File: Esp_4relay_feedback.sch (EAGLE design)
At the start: 58 parts, among them IC1 LM1117MP-3.3, IC2 7805TV, IC3 7805TV, IC4 7805TV, K1 G5LE, K2 G5LE, K3 G5LE, K4 G5LE, Q1 16MHz, SW1 Push Switch, T1 BC547, T2 BC547, T3 BC547, T4 BC547, U2 ATMEGA328P_PDIP

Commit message: added 8 relays
8 relays arranged in 4 up-down manner with
esp and atmega328 at left side.

routing 70% completed.
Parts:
- removed C7, C8: 10uf, rcl:CPOL-USE2.5-6
- removed IC2: 7805TV, linear:7805TV
- removed JP5: (no value), pinhead:PINHD-1X6
- added D5, D6, D7, D8: 1N4007, diode:1N4004
- added K5, K6, K7, K8: G5LE, relay:G5LE
- added OK5, OK6, OK7, OK8: PC817, optocoupler:PC817
- added R10, R16, R18, R20: 220k, rcl:R-US_0207/10
- added R13, R17, R19, R7: 1k, rcl:R-US_0207/10
- added T5, T6, T7, T8: BC547, transistor:BC547
- added X10, X8, X9: (no value), con-wago-500:W237-103
- X5: device con-wago-500:W237-102 -> con-wago-500:W237-103; MPN (none) -> 237-103; OC_FARNELL (none) -> unknown; OC_NEWARK (none) -> 18M7116
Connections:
- removed net ESP_SUPPLY: C2.+, C8.+, IC1.IN, IC2.VO
- new net F5: OK5.COL, U2.PC3(ADC3)
- new net F6: OK6.COL, U2.PD4(XCK/T0)
- new net F7: OK7.COL, U2.PC5(ADC5/SCL)
- new net F8: OK8.COL, U2.PD2(INT0)
- new net N$34: OK5.C, R10.2
- new net N$35: R7.1, T5.B
- new net N$46: D5.A, K51.2, T5.C
- new net N$47: K62.P, OK6.A, X8-2.KL
- new net N$48: K62.S, R16.1, X8-1.KL
- new net N$49: OK6.C, R16.2
- new net N$50: R13.1, T6.B
- new net N$51: D6.A, K61.2, T6.C
- new net N$52: K72.P, OK7.A, X9-2.KL
- new net N$53: K72.S, R18.1, X9-1.KL
- new net N$54: OK7.C, R18.2
- new net N$55: R17.1, T7.B
- new net N$56: D7.A, K71.2, T7.C
- new net N$57: K82.P, OK8.A, X10-2.KL
- new net N$58: K82.S, R20.1, X10-1.KL
- new net N$59: OK8.C, R20.2
- new net N$60: R19.1, T8.B
- new net N$61: D8.A, K81.2, T8.C
- new net N$62: K52.O, X5-3.KL
- new net N$63: K62.O, X8-3.KL
- new net N$64: K72.O, X9-3.KL
- new net N$65: K82.O, X10-3.KL
- new net R5: R7.2, U2.PC2(ADC2)
- new net R6: R13.2, U2.PD5(T1)
- new net R7: R17.2, U2.PC4(ADC4/SDA)
- new net R8: R19.2, U2.PD3(INT1)
- net F1: now also U2.PB4(MISO); no longer U2.PD3(INT1)
- net F2: now also U2.PB0(ICP); no longer U2.PD5(T1)
- net F3: now also U2.PC1(ADC1); no longer U2.PD7(AIN1)
- net F4: now also U2.PD6(AIN0); no longer U2.PB1(OC1A)
- net GND: now also OK5.EMIT, OK6.EMIT, OK7.EMIT, OK8.EMIT, T5.E, T6.E, T7.E, T8.E; no longer C7.-, C8.-, IC2.GND, JP5.6, X5-2.KL
- net N$16: now also K52.P, OK5.A, X5-2.KL; no longer JP5.3, U2.PB5(SCK)
- net N$23: now also U2.PB2(SS/OC1B); no longer JP5.2, U2.PB4(MISO)
- net N$26: now also U2.PB3(MOSI/OC2); no longer C7.+, IC2.VI, X5-1.KL
- net N$32: now also K52.S, R10.1, X5-1.KL; no longer JP5.1, U2.PB3(MOSI/OC2)
- net R1: now also U2.PB5(SCK); no longer U2.PD2(INT0)
- net R2: now also U2.PB1(OC1A); no longer U2.PD4(XCK/T0)
- net R3: now also U2.PC0(ADC0); no longer U2.PD6(AIN0)
- net R4: now also U2.PD7(AIN1); no longer U2.PB0(ICP)
- net RELAY_SUPPLY: now also D5.C, D6.C, D7.C, D8.C, K51.1, K61.1, K71.1, K81.1
- net RESET: no longer JP5.4
- net VCC: now also C2.+, IC1.IN; no longer JP5.5

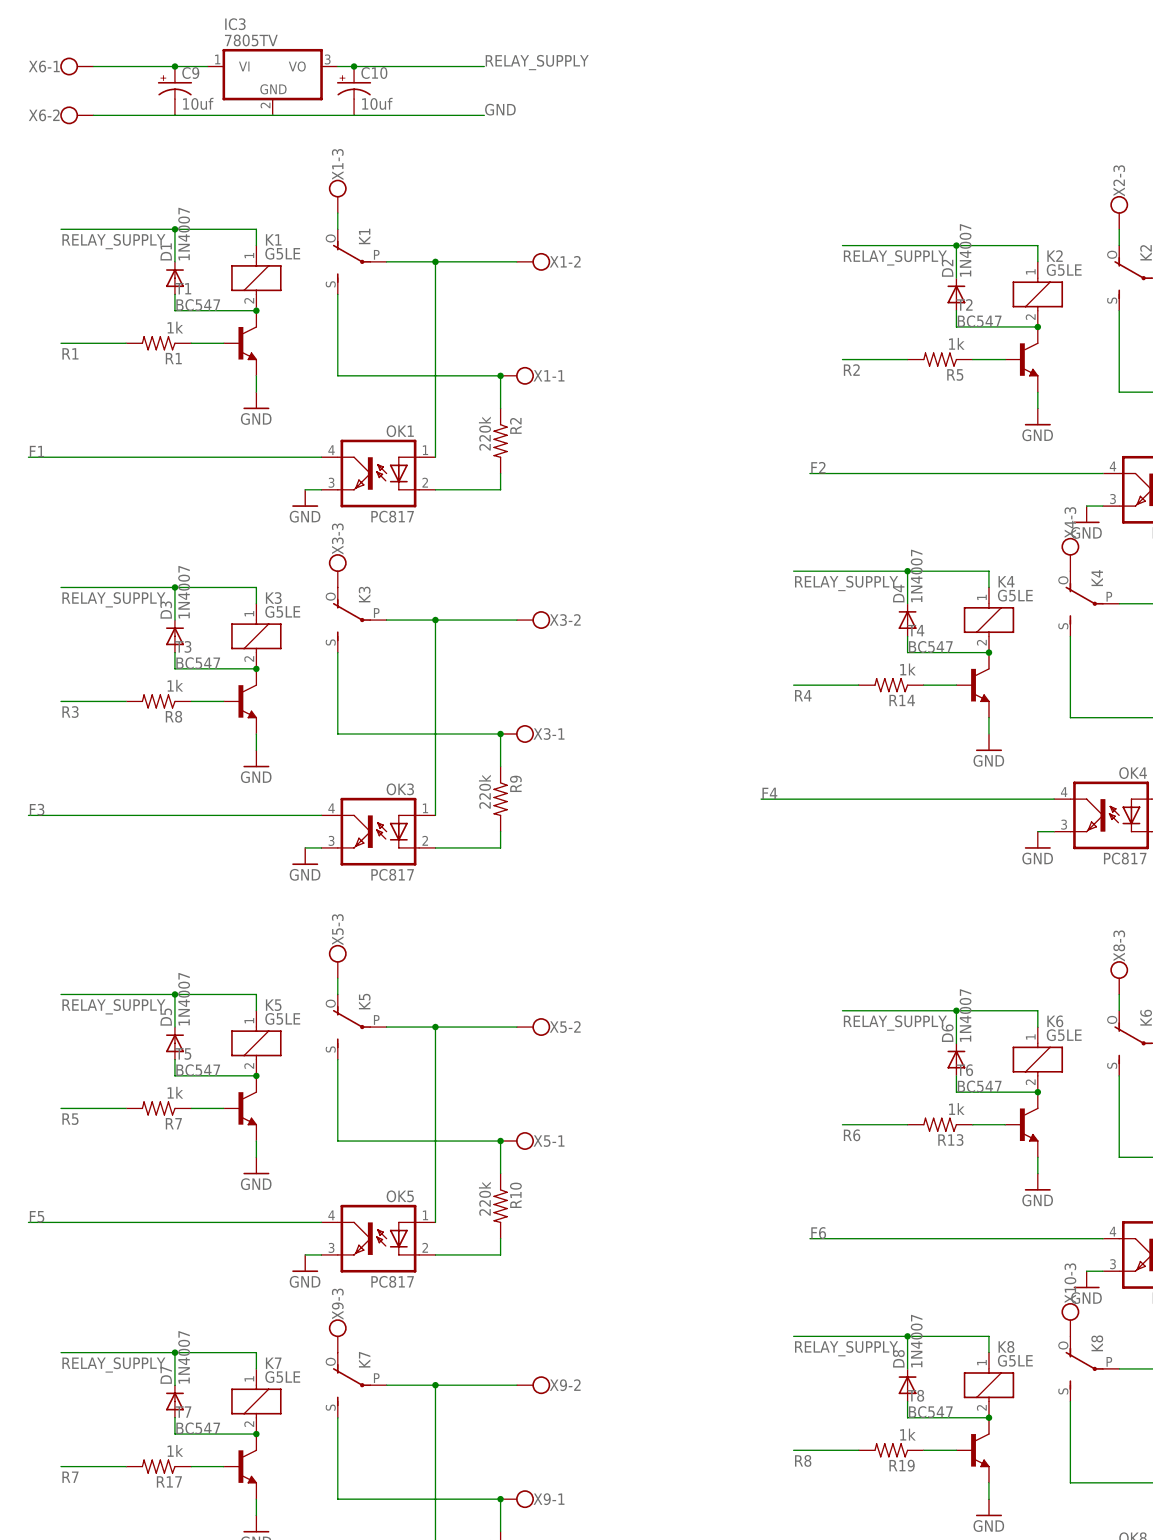
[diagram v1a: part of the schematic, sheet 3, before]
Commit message: component placing changed
Controller and esp placed in between relays.
routing done
PCB size : 130X95mm
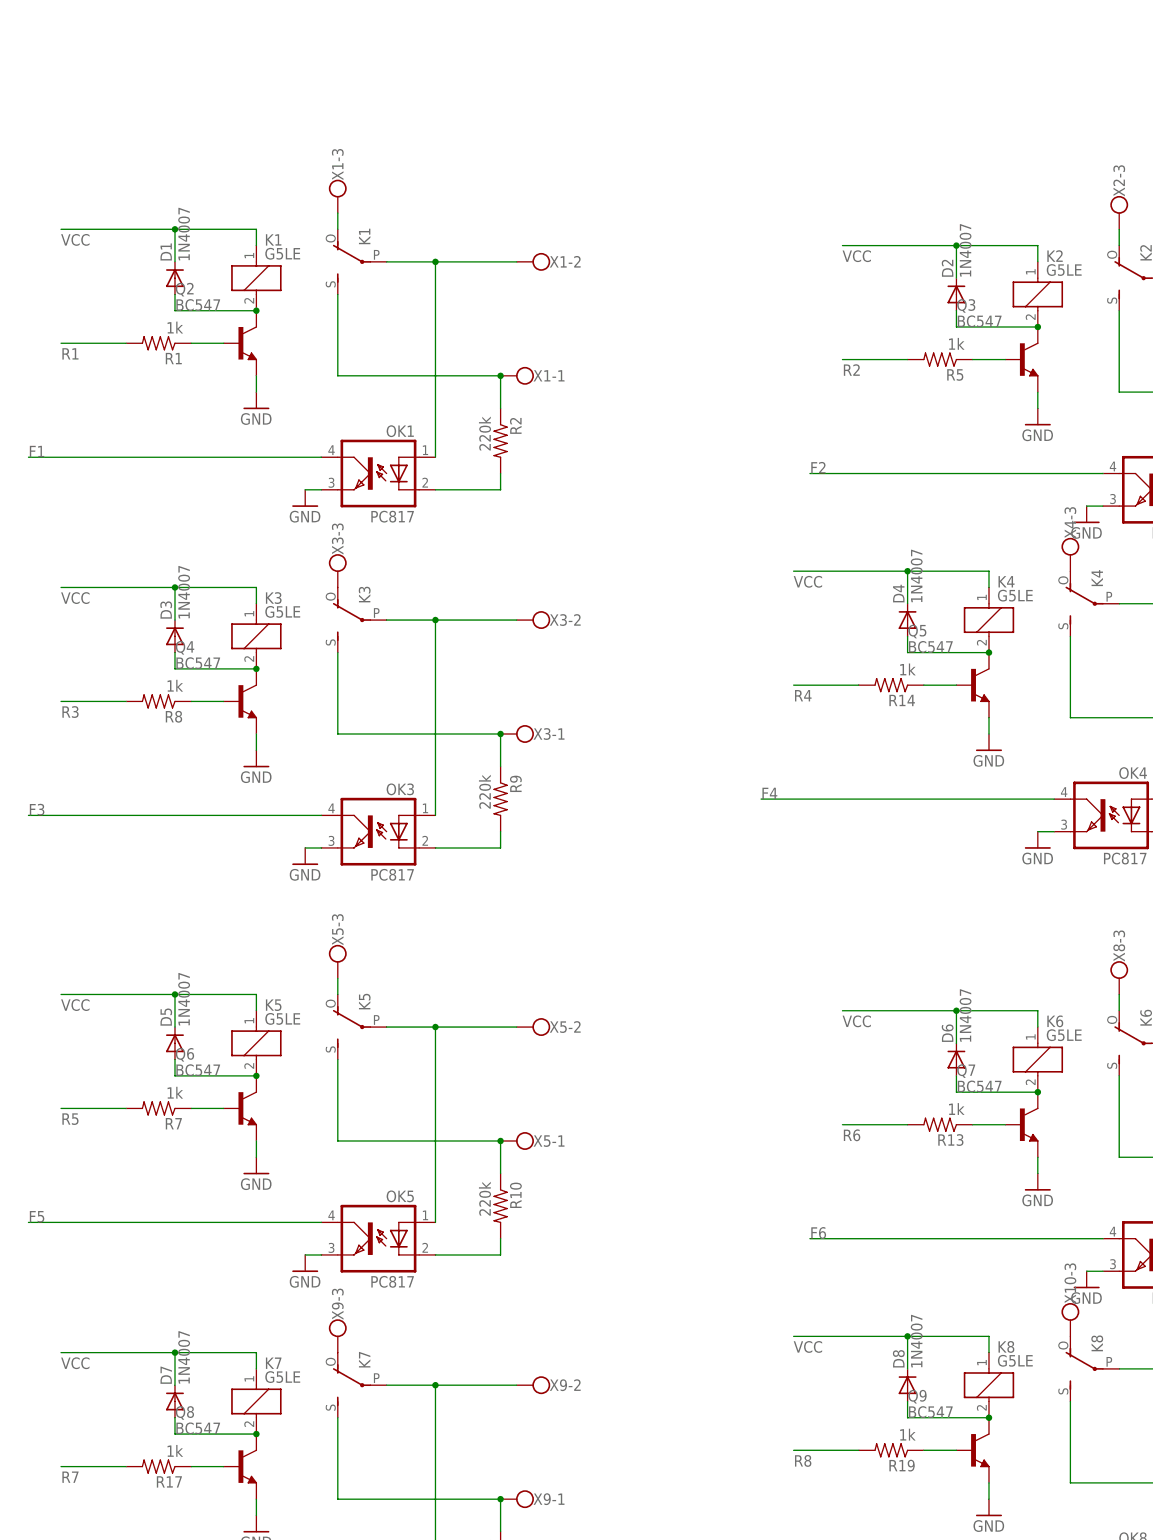
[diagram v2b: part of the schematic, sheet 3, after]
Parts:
- removed C10, C9: 10uf, rcl:CPOL-USE2.5-6
- removed IC3: 7805TV, linear:7805TV
- removed SW1: Push Switch, adafruit:SWITCH_PUSHBUTTONEVQ-PE
- removed T1, T2, T3, T4, T5, T6, T7, T8: BC547, transistor:BC547
- removed X6: (no value), con-wago-500:W237-102
- added Q2, Q3, Q4, Q5, Q6, Q7, Q8, Q9: BC547, transistor-npn:BC447
- added S1: (no value), switch-omron:10-XX
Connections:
- removed net N$23: U2.PB2(SS/OC1B)
- removed net N$26: U2.PB3(MOSI/OC2)
- removed net N$27: C9.+, IC3.VI, X6-1.KL
- removed net RELAY_SUPPLY: C10.+, D1.C, D2.C, D3.C, D4.C, D5.C, D6.C, D7.C, D8.C, IC3.VO, K11.1, K21.1, K31.1, K41.1, K51.1, K61.1, K71.1, K81.1
- new net ERT: U2.PC0(ADC0)
- new net WE: U2.PC1(ADC1)
- net F1: now also U2.PD6(AIN0); no longer U2.PB4(MISO)
- net F2: now also U2.PD5(T1); no longer U2.PB0(ICP)
- net F3: now also U2.PB0(ICP); no longer U2.PC1(ADC1)
- net F4: now also U2.PD3(INT1); no longer U2.PD6(AIN0)
- net F5: now also U2.PB3(MOSI/OC2); no longer U2.PC3(ADC3)
- net F6: now also U2.PC4(ADC4/SDA); no longer U2.PD4(XCK/T0)
- net F7: now also U2.PB5(SCK); no longer U2.PC5(ADC5/SCL)
- net F8: now also U2.PC2(ADC2); no longer U2.PD2(INT0)
- net GND: now also Q2.E, Q3.E, Q4.E, Q5.E, Q6.E, Q7.E, Q8.E, Q9.E, S1.P, S1.P1; no longer C10.-, C9.-, IC3.GND, SW1.P$1, T1.E, T2.E, T3.E, T4.E, T5.E, T6.E, T7.E, T8.E, X6-2.KL
- net N$11: now also Q3.B; no longer T2.B
- net N$12: now also Q3.C; no longer T2.C
- net N$17: now also Q4.B; no longer T3.B
- net N$18: now also Q4.C; no longer T3.C
- net N$24: now also Q5.B; no longer T4.B
- net N$25: now also Q5.C; no longer T4.C
- net N$35: now also Q6.B; no longer T5.B
- net N$46: now also Q6.C; no longer T5.C
- net N$50: now also Q7.B; no longer T6.B
- net N$51: now also Q7.C; no longer T6.C
- net N$55: now also Q8.B; no longer T7.B
- net N$56: now also Q8.C; no longer T7.C
- net N$60: now also Q9.B; no longer T8.B
- net N$61: now also Q9.C; no longer T8.C
- net N$7: now also Q2.B; no longer T1.B
- net N$8: now also Q2.C; no longer T1.C
- net R1: now also U2.PD7(AIN1); no longer U2.PB5(SCK)
- net R2: now also U2.PD4(XCK/T0); no longer U2.PB1(OC1A)
- net R3: now also U2.PB1(OC1A); no longer U2.PC0(ADC0)
- net R4: now also U2.PD2(INT0); no longer U2.PD7(AIN1)
- net R5: now also U2.PB2(SS/OC1B); no longer U2.PC2(ADC2)
- net R6: now also U2.PC5(ADC5/SCL); no longer U2.PD5(T1)
- net R7: now also U2.PB4(MISO); no longer U2.PC4(ADC4/SDA)
- net R8: now also U2.PC3(ADC3); no longer U2.PD3(INT1)
- net RESET: now also S1.S, S1.S1; no longer SW1.P$2
- net VCC: now also D1.C, D2.C, D3.C, D4.C, D5.C, D6.C, D7.C, D8.C, K11.1, K21.1, K31.1, K41.1, K51.1, K61.1, K71.1, K81.1

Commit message: polygon added.
polygon added.
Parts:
- R11, R12, R4: value (none) -> 10k
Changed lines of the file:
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@@
 <parts>
 <part name="U$1" library="esp826612q" deviceset="ESP12Q" device=""/>
-<part name="R4" library="rcl" deviceset="R-US_" device="0207/10"/>
-<part name="R11" library="rcl" deviceset="R-US_" device="0207/10"/>
-<part name="R12" library="rcl" deviceset="R-US_" device="0207/10"/>
+<part name="R4" library="rcl" deviceset="R-US_" device="0207/10" value="10k"/>
+<part name="R11" library="rcl" deviceset="R-US_" device="0207/10" value="10k"/>
+<part name="R12" library="rcl" deviceset="R-US_" device="0207/10" value="10k"/>
 <part name="JP6" library="pinhead" deviceset="PINHD-1X2" device=""/>
 <part name="IC1" library="lm1117_10" deviceset="LM1117?-*" device="MP" technology="3.3"/>

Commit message: feature added
added power on delay for relay supply.
added logic level for esp to atmega328 communication.
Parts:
- removed JP9: (no value), pinhead:PINHD-1X2
- added C7: 0.01uf, rcl:C-US025-025X050
- added C8: 10uf, rcl:CPOL-USE2.5-6
- added C9: 100uf, rcl:CPOL-USE2.5-6
- added IC2: NE555, st-microelectronics:NE555
- added JP1: (no value), pinhead:PINHD-1X2
- added Q11: BC450, transistor-pnp:BC450
- added R21: 47k, rcl:R-US_0207/10
- added R22, R23: 1k, rcl:R-US_0207/10
- added R24, R25, R26, R27: 10k, rcl:R-US_0207/10
- added T1, T2: 2N7000, transistor:BC547-NPN-TO92-CBE
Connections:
- new net N$23: JP1.1, R27.2, T2.E
- new net N$26: C9.+, IC2.DIS, IC2.TRE, R21.1
- new net N$27: JP8.1, R25.2, T1.E
- new net N$36: C8.+, IC2.TRI, R22.1
- new net N$37: C7.1, IC2.CON
- new net N$38: IC2.OUT, R23.2
- new net N$39: Q11.B, R23.1
- new net RELAY_SUPPLY: D1.C, D2.C, D3.C, D4.C, D5.C, D6.C, D7.C, D8.C, K11.1, K21.1, K31.1, K41.1, K51.1, K61.1, K71.1, K81.1, Q11.C
- net 3V3: now also R24.1, R26.1, T1.B, T2.B
- net GND: now also C7.2, C8.-, C9.-, IC2.GND
- net RX: now also JP1.2; no longer JP9.2
- net RX1: now also R24.2, T1.C; no longer JP8.1
- net TX1: now also R26.2, T2.C; no longer JP9.1
- net VCC: now also IC2./RES, IC2.VCC+, Q11.E, R21.2, R22.2, R25.1, R27.1; no longer D1.C, D2.C, D3.C, D4.C, D5.C, D6.C, D7.C, D8.C, K11.1, K21.1, K31.1, K41.1, K51.1, K61.1, K71.1, K81.1

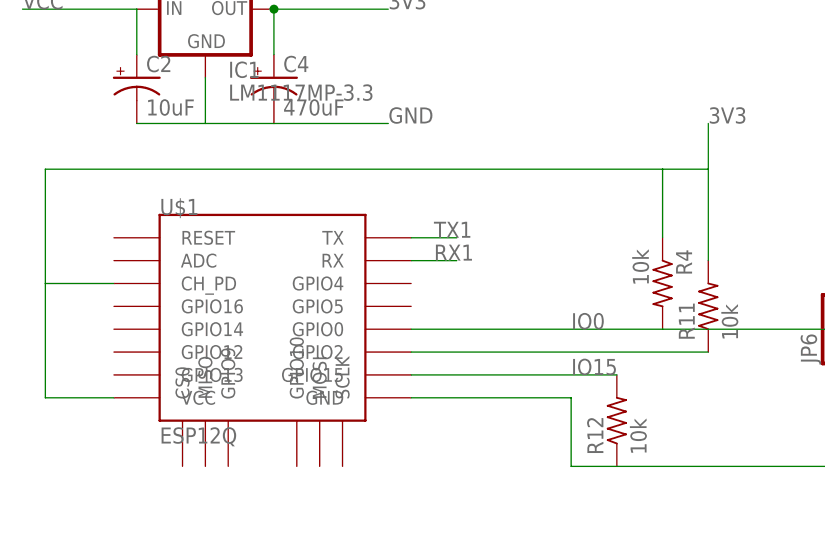
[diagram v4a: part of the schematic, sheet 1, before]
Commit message: Esp pull up added
pull up for reset and chpd.
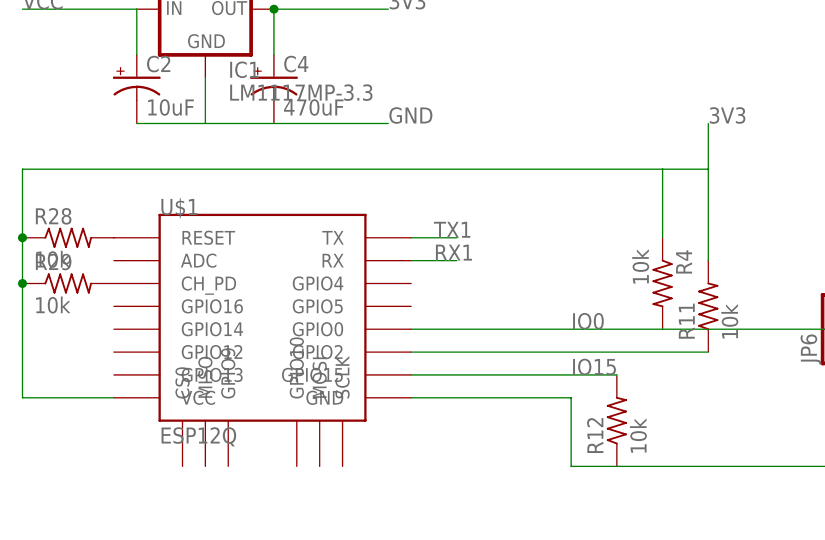
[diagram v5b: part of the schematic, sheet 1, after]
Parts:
- added R28, R29: 10k, rcl:R-US_0207/10
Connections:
- new net N$40: R29.2, U$1.CH_PD
- new net N$41: R28.2, U$1.RESET
- net 3V3: now also R28.1, R29.1; no longer U$1.CH_PD
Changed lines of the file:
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@@
 <part name="R26" library="rcl" deviceset="R-US_" device="0207/10" value="10k"/>
 <part name="R27" library="rcl" deviceset="R-US_" device="0207/10" value="10k"/>
+<part name="R28" library="rcl" deviceset="R-US_" device="0207/10" value="10k"/>
+<part name="R29" library="rcl" deviceset="R-US_" device="0207/10" value="10k"/>
 </parts>
 <sheets>
@@
 <instance part="R26" gate="G$1" x="152.4" y="17.78" rot="R90"/>
 <instance part="R27" gate="G$1" x="172.72" y="17.78" rot="R90"/>
+<instance part="R28" gate="G$1" x="17.78" y="35.56"/>
+<instance part="R29" gate="G$1" x="17.78" y="30.48"/>
 </instances>
 <busses>
@@
 <wire x1="88.9" y1="43.18" x2="88.9" y2="48.26" width="0.1524" layer="91"/>
 <label x="88.9" y="48.26" size="1.778" layer="95"/>
-<pinref part="U$1" gate="G$1" pin="CH_PD"/>
-<wire x1="22.86" y1="30.48" x2="15.24" y2="30.48" width="0.1524" layer="91"/>
-<wire x1="15.24" y1="30.48" x2="15.24" y2="43.18" width="0.1524" layer="91"/>
-<wire x1="15.24" y1="43.18" x2="83.82" y2="43.18" width="0.1524" layer="91"/>
+<wire x1="12.7" y1="43.18" x2="83.82" y2="43.18" width="0.1524" layer="91"/>
 <pinref part="U$1" gate="G$1" pin="VCC"/>
-<wire x1="22.86" y1="17.78" x2="15.24" y2="17.78" width="0.1524" layer="91"/>
-<wire x1="15.24" y1="17.78" x2="15.24" y2="30.48" width="0.1524" layer="91"/>
+<wire x1="22.86" y1="17.78" x2="12.7" y2="17.78" width="0.1524" layer="91"/>
+<wire x1="12.7" y1="17.78" x2="12.7" y2="30.48" width="0.1524" layer="91"/>
+<pinref part="R29" gate="G$1" pin="1"/>
+<wire x1="12.7" y1="30.48" x2="12.7" y2="35.56" width="0.1524" layer="91"/>
+<junction x="12.7" y="30.48"/>
+<pinref part="R28" gate="G$1" pin="1"/>
+<wire x1="12.7" y1="35.56" x2="12.7" y2="43.18" width="0.1524" layer="91"/>
+<junction x="12.7" y="35.56"/>
 </segment>
 <segment>
@@
 </segment>
 </net>
+<net name="N$40" class="0">
+<segment>
+<pinref part="U$1" gate="G$1" pin="CH_PD"/>
+<pinref part="R29" gate="G$1" pin="2"/>
+</segment>
+</net>
+<net name="N$41" class="0">
+<segment>
+<pinref part="U$1" gate="G$1" pin="RESET"/>
+<pinref part="R28" gate="G$1" pin="2"/>
+</segment>
+</net>
